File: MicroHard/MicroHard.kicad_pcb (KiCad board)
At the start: 6 copper layers, 198.2 x 104.1 mm, 193 parts, among them IC1 IS66WVO32M8DBLL-166BLI, J1 USB_B_Micro, J2 Micro_SD_Card_Det2, J3 GPIO_header, J4 MCU_Debug, J5 Controller Connector, J6 FPGA_GPIO_header, J7 FPGA_DEBUG, J8 L77HDE15SD1CH4FVGA, SW1 KMR221NGLFS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

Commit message: final fix
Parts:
- moved C35 25.1 mm to (123.2, 106.8)
- moved C44 14.4 mm to (113.4, 108.7), turned to 180 degrees
- moved C57 10.4 mm to (110.6, 95.9)
- moved C61 1.67 mm to (113.3, 101.2), turned to 90 degrees
- moved C55 0.25 mm to (114.4, 105.7)
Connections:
- U4 pad G10: +1V8 -> GND
- U4 pad G8: +1V8 -> GND
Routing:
- net +1V8: track 81.9 -> 96.7 mm
- net FPGA_CONFIG_CLOCK: track 34.2 -> 45.8 mm, vias 2 -> 4
- net FPGA_RESET: track 123.3 -> 132.5 mm
- net INIT: track 17.3 -> 25.0 mm
- net GND: track 253.8 -> 259.6 mm, vias 138 -> 136
- net Net-(U3B-PA2): track 42.9 -> 46.6 mm
- net FPGA_DONE: track 112.9 -> 115.4 mm
- net +3.3V: track 170.4 -> 172.8 mm
- net /FPGA/Unit A/Flash Memory/FLASH_CS#: track 20.1 -> 21.4 mm
- net +1V0: track 52.9 -> 53.3 mm, vias 18 -> 19

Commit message: Final changes
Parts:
- J4: footprint Connector_PinHeader_1.00mm:PinHeader_2x10_P1.00mm_Vertical -> Connector_IDC:IDC-Header_2x10_P2.54mm_Vertical
- moved R15 11.8 mm to (217.7, 77.9)
- moved SW3 11.8 mm to (212.7, 77.9)
- moved J3 10.3 mm to (229.5, 126.9)
- moved J4 9.13 mm to (225.2, 77.3)
- moved C82 5.95 mm to (219.0, 136.8)
- moved J2 5.95 mm to (223.8, 138.8)
- moved R78 5.95 mm to (212.3, 133.6)
- moved R77 5.45 mm to (211.2, 145.5), turned to 180 degrees
- moved J5 4.25 mm to (187.9, 144.8)
- moved C10 3.05 mm to (52.9, 143.3)
- moved C11 3.05 mm to (49.6, 143.3)
- moved C13 3.05 mm to (53.8, 138.8)
- moved C14 3.05 mm to (53.9, 131.8)
- moved C15 3.05 mm to (70.1, 143.3)
- moved C16 3.05 mm to (66.3, 143.3)
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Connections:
- U4 pad G10: GND -> +1V8
- U4 pad G8: GND -> +1V8
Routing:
- net Net-(J3-Pin_7): track 25.3 -> 33.2 mm
- net SD_US2_CLK: track 42.5 -> 48.7 mm
- net SD_US2_RX: track 44.7 -> 50.8 mm
- net SD_US2_CS: track 42.7 -> 48.7 mm
- net SD_US2_TX: track 42.7 -> 48.7 mm
- net Net-(U3B-PB14): track 12.0 -> 16.7 mm
- net US1_CS: track 43.0 -> 47.6 mm
- net US1_CLK: track 43.4 -> 48.1 mm
- net Net-(J6-Pin_2): track 49.0 -> 44.3 mm
- net Net-(J3-Pin_6): track 28.7 -> 33.3 mm
- net Net-(J3-Pin_5): track 29.2 -> 33.5 mm
- net Controller_Btn1: track 26.8 -> 31.1 mm
- net Controller_Z: track 33.1 -> 37.4 mm
- net Controller_X: track 34.1 -> 38.4 mm
- net Controller_Y: track 32.8 -> 37.0 mm
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- added copper zone on F.Cu, net GND
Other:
- board size 198.2 x 104.1 mm -> 197.5 x 107.7 mm
- board text added: "*"

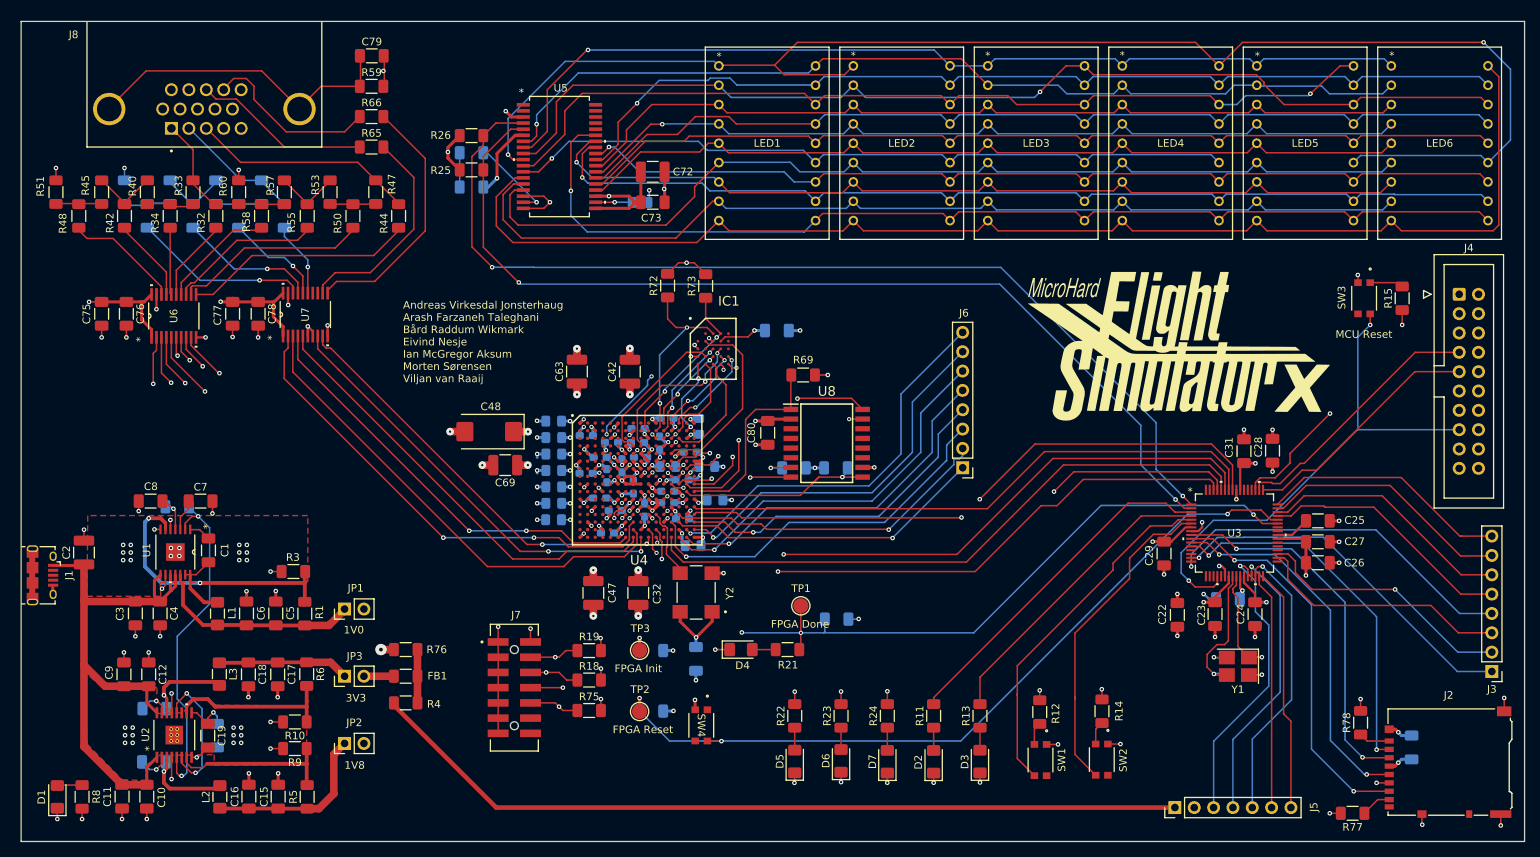
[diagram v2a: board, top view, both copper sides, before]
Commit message: Change inductor footprint
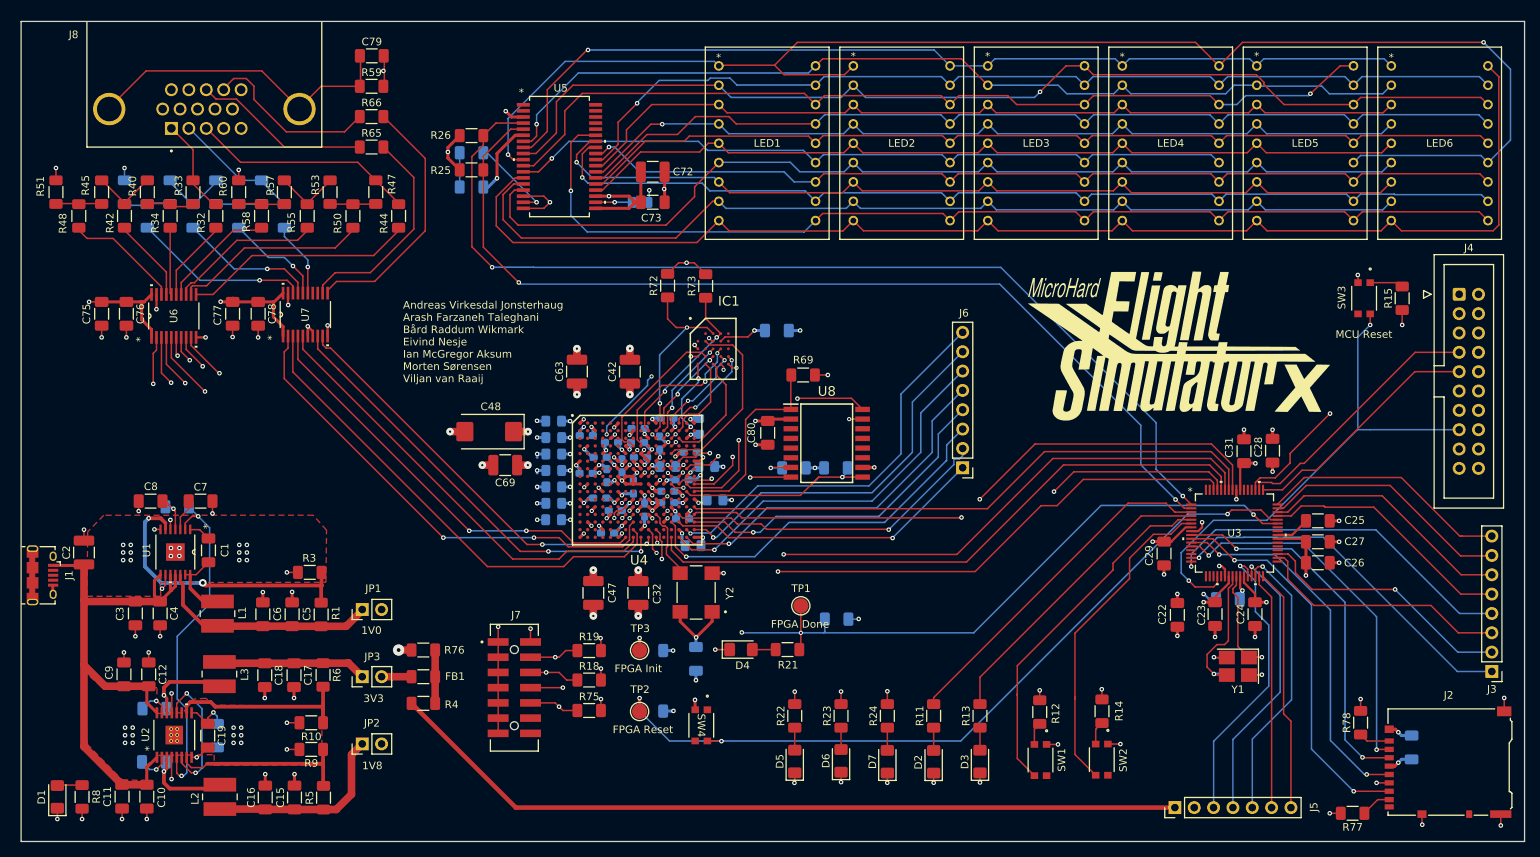
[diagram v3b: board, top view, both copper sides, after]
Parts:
- L1, L2, L3: footprint Inductor_SMD:L_1206_3216Metric_Pad1.42x1.75mm_HandSolder -> 74438357022 Wuerth Inductor:IND_8357022_WRE
- moved JP1 2.32 mm to (81.2, 118.7)
- moved JP2 2.32 mm to (81.2, 136.4)
- moved JP3 2.32 mm to (81.2, 127.6)
- moved FB1 2.32 mm to (89.2, 127.6)
- moved R4 2.32 mm to (89.2, 131.1)
- moved R76 2.32 mm to (89.2, 124.1)
- moved C15 2.15 mm to (72.3, 143.4)
- moved C16 2.15 mm to (68.4, 143.4)
- moved R10 2.15 mm to (74.5, 133.6)
- moved R9 2.15 mm to (74.5, 137.1)
- moved C17 2.15 mm to (72.2, 127.4)
- moved C18 2.15 mm to (68.3, 127.4)
- moved C5 2.15 mm to (71.9, 119.4)
- moved C6 2.15 mm to (68.1, 119.4)
- moved R1 2.15 mm to (75.8, 119.4)
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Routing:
- net Net-(JP2-A): track 23.0 -> 26.4 mm
- net Net-(JP1-A): track 27.4 -> 30.3 mm
- net Net-(JP3-A): track 17.2 -> 19.8 mm
- net +3.3VA: track 108.1 -> 105.6 mm
- net Net-(U1-PG): track 35.7 -> 38.1 mm
- net Net-(U2-VFB1): track 21.8 -> 24.0 mm
- net Net-(U2-VFB2): track 22.2 -> 24.0 mm
- net +1V0: track 55.7 -> 54.8 mm
- net +1V8: track 99.7 -> 100.5 mm
- net Net-(U2-SW2): track 13.5 -> 12.8 mm

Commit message: Small fixes
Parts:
- C79: footprint Capacitor_SMD:C_1206_3216Metric_Pad1.33x1.80mm_HandSolder -> Capacitor_SMD:C_0805_2012Metric_Pad1.18x1.45mm_HandSolder
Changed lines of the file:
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@@
 		)
 		(fp_text user "*"
-			(at -0.0112 -1.3 0)
+			(at -0.0212 -1.47 0)
 			(layer "F.SilkS")
 			(effects
@@
 		(fp_text user "*"
 			(at 0 -1.693333 0)
-			(unlocked yes)
 			(layer "F.Fab")
 			(effects
@@
 		(fp_text user "*"
 			(at 0 -1.693333 0)
+			(unlocked yes)
 			(layer "F.Fab")
 			(effects
@@
 		)
 		(fp_text user "*"
-			(at -0.0316 -1.1 0)
+			(at 0.0284 -1.21 0)
 			(layer "F.SilkS")
 			(effects
@@
 			)
 		)
-		(fp_text user "${REFERENCE}"
-			(at 6.35 10.16 0)
+		(fp_text user "*"
+			(at 0 -1.693333 0)
 			(unlocked yes)
 			(layer "F.Fab")
@@
 		(fp_text user "*"
 			(at 0 -1.693333 0)
-			(unlocked yes)
 			(layer "F.Fab")
 			(effects
@@
 			)
 		)
-		(fp_text user "*"
-			(at 0 -1.693333 0)
+		(fp_text user "${REFERENCE}"
+			(at 6.35 10.16 0)
+			(unlocked yes)
 			(layer "F.Fab")
 			(effects
@@
 		)
 		(fp_text user "*"
-			(at -0.0188 -1.2 0)
+			(at -0.0188 -1.47 0)
 			(layer "F.SilkS")
 			(effects
@@
 		(fp_text user "*"
 			(at 0 -1.693333 0)
+			(unlocked yes)
 			(layer "F.Fab")
 			(effects
@@
 		(fp_text user "*"
 			(at 0 -1.693333 0)
-			(unlocked yes)
 			(layer "F.Fab")
 			(effects
@@
 		)
 		(fp_text user "*"
-			(at -0.0036 -1.11 0)
+			(at -0.0436 -1.3 0)
 			(layer "F.SilkS")
 			(effects
@@
 			)
 		)
-		(fp_text user "*"
-			(at 0 -1.693333 0)
+		(fp_text user "${REFERENCE}"
+			(at 6.35 10.16 0)
 			(unlocked yes)
 			(layer "F.Fab")
@@
 		(fp_text user "*"
 			(at 0 -1.693333 0)
+			(unlocked yes)
 			(layer "F.Fab")
 			(effects
@@
 			)
 		)
-		(fp_text user "${REFERENCE}"
-			(at 6.35 10.16 0)
-			(unlocked yes)
+		(fp_text user "*"
+			(at 0 -1.693333 0)
 			(layer "F.Fab")
 			(effects
@@
 		)
 		(fp_text user "*"
-			(at -0.014 -1.27 0)
-			(unlocked yes)
+			(at 0 -1.31 0)
 			(layer "F.SilkS")
 			(effects
@@
 		)
 		(fp_text user "*"
-			(at -0.0164 -1.27 0)
+			(at -0.0164 -1.42 0)
 			(layer "F.SilkS")
 			(effects
@@
 		(fp_text user "*"
 			(at 0 -1.693333 0)
+			(unlocked yes)
 			(layer "F.Fab")
 			(effects
@@
 			)
 		)
-		(fp_text user "${REFERENCE}"
-			(at 6.35 10.16 0)
-			(unlocked yes)
+		(fp_text user "*"
+			(at 0 -1.693333 0)
 			(layer "F.Fab")
 			(effects
@@
 			)
 		)
-		(fp_text user "*"
-			(at 0 -1.693333 0)
+		(fp_text user "${REFERENCE}"
+			(at 6.35 10.16 0)
 			(unlocked yes)
 			(layer "F.Fab")
@@
 		)
 	)
-	(footprint "Capacitor_SMD:C_1206_3216Metric_Pad1.33x1.80mm_HandSolder"
+	(footprint "Capacitor_SMD:C_0805_2012Metric_Pad1.18x1.45mm_HandSolder"
 		(layer "F.Cu")
 		(at 82.405 46.0225)
-		(descr "Capacitor SMD 1206 (3216 Metric), square (rectangular) end terminal, IPC_7351 nominal with elongated pad for handsoldering. (Body size source: IPC-SM-782 page 76, https://www.pcb-3d.com/wordpress/wp-content/uploads/ipc-sm-782a_amendment_1_and_2.pdf), generated with kicad-footprint-generator")
+		(descr "Capacitor SMD 0805 (2012 Metric), square (rectangular) end terminal, IPC_7351 nominal with elongated pad for handsoldering. (Body size source: IPC-SM-782 page 76, https://www.pcb-3d.com/wordpress/wp-content/uploads/ipc-sm-782a_amendment_1_and_2.pdf, https://docs.google.com/spreadsheets/d/1BsfQQcO9C6DZCsRaXUlFlo91Tg2WpOkGARC1WS5S8t0/edit?usp=sharing), generated with kicad-footprint-generator")
 		(tags "capacitor handsolder")
 		(property "Reference" "C79"
-			(at 0 -1.85 0)
+			(at 0 -1.68 0)
 			(layer "F.SilkS")
 			(effects
@@
 		)
 		(property "Value" "4p"
-			(at 0 1.85 0)
+			(at 0 1.68 0)
 			(layer "F.Fab")
 			(effects
@@
 			)
 		)
-		(property "Footprint" "Capacitor_SMD:C_1206_3216Metric_Pad1.33x1.80mm_HandSolder"
+		(property "Footprint" "Capacitor_SMD:C_0805_2012Metric_Pad1.18x1.45mm_HandSolder"
 			(at 0 0 0)
 			(unlocked yes)
@@
 		(attr smd)
 		(fp_line
-			(start -0.711252 -0.91)
-			(end 0.711252 -0.91)
+			(start -0.261252 -0.735)
+			(end 0.261252 -0.735)
 			(stroke
 				(width 0.12)
@@
 		)
 		(fp_line
-			(start -0.711252 0.91)
-			(end 0.711252 0.91)
+			(start -0.261252 0.735)
+			(end 0.261252 0.735)
 			(stroke
 				(width 0.12)
@@
 		)
 		(fp_line
-			(start -2.48 -1.15)
-			(end 2.48 -1.15)
+			(start -1.88 -0.98)
+			(end 1.88 -0.98)
 			(stroke
 				(width 0.05)
@@
 		)
 		(fp_line
-			(start -2.48 1.15)
-			(end -2.48 -1.15)
+			(start -1.88 0.98)
+			(end -1.88 -0.98)
 			(stroke
 				(width 0.05)
@@
 		)
 		(fp_line
-			(start 2.48 -1.15)
-			(end 2.48 1.15)
+			(start 1.88 -0.98)
+			(end 1.88 0.98)
 			(stroke
 				(width 0.05)
@@
 		)
 		(fp_line
-			(start 2.48 1.15)
-			(end -2.48 1.15)
+			(start 1.88 0.98)
+			(end -1.88 0.98)
 			(stroke
 				(width 0.05)
@@
 		)
 		(fp_line
-			(start -1.6 -0.8)
-			(end 1.6 -0.8)
+			(start -1 -0.625)
+			(end 1 -0.625)
 			(stroke
 				(width 0.1)
@@
 		)
 		(fp_line
-			(start -1.6 0.8)
-			(end -1.6 -0.8)
+			(start -1 0.625)
+			(end -1 -0.625)
 			(stroke
 				(width 0.1)
@@
 		)
 		(fp_line
-			(start 1.6 -0.8)
-			(end 1.6 0.8)
+			(start 1 -0.625)
+			(end 1 0.625)
 			(stroke
 				(width 0.1)
@@
 		)
 		(fp_line
-			(start 1.6 0.8)
-			(end -1.6 0.8)
+			(start 1 0.625)
+			(end -1 0.625)
 			(stroke
 				(width 0.1)
@@
 			(effects
 				(font
-					(size 0.8 0.8)
-					(thickness 0.12)
+					(size 0.5 0.5)
+					(thickness 0.08)
 				)
 			)
 		)
 		(pad "1" smd roundrect
-			(at -1.5625 0)
-			(size 1.325 1.8)
+			(at -1.0375 0)
+			(size 1.175 1.45)
 			(layers "F.Cu" "F.Paste" "F.Mask")
-			(roundrect_rratio 0.188679)
+			(roundrect_rratio 0.212766)
 			(net 19 "Net-(J8-SHIELD)")
 			(pintype "passive")
 		)
 		(pad "2" smd roundrect
-			(at 1.5625 0)
-			(size 1.325 1.8)
+			(at 1.0375 0)
+			(size 1.175 1.45)
 			(layers "F.Cu" "F.Paste" "F.Mask")
-			(roundrect_rratio 0.188679)
+			(roundrect_rratio 0.212766)
 			(net 2 "GND")
 			(pintype "passive")
 		)
-		(model "${KICAD8_3DMODEL_DIR}/Capacitor_SMD.3dshapes/C_1206_3216Metric.wrl"
+		(model "${KICAD8_3DMODEL_DIR}/Capacitor_SMD.3dshapes/C_0805_2012Metric.wrl"
 			(offset
 				(xyz 0 0 0)
@@
 	)
 	(segment
+		(start 83.4425 46.0225)
+		(end 83.925 46.505)
+		(width 0.2)
+		(layer "F.Cu")
+		(net 2)
+	)
+	(segment
 		(start 125.875 109.25)
 		(end 124.75 109.25)
@@
 	)
 	(segment
+		(start 83.925 46.505)
+		(end 83.925 48)
+		(width 0.2)
+		(layer "F.Cu")
+		(net 2)
+	)
+	(segment
 		(start 67.475 83)
 		(end 67.475 81.4625)
@@
 	)
 	(segment
-		(start 84.04945 46.0225)
-		(end 84.04945 47.87555)
-		(width 0.2)
-		(layer "F.Cu")
-		(net 2)
-	)
-	(segment
 		(start 193.150002 122.3441)
 		(end 193.150001 122.344101)
@@
 	)
 	(segment
-		(start 84.04945 47.87555)
-		(end 83.925 48)
-		(width 0.2)
-		(layer "F.Cu")
-		(net 2)
-	)
-	(segment
 		(start 114.76 103.25)
 		(end 114.75 103.25)
@@
 	)
 	(segment
-		(start 75.73425 50.0225)
-		(end 72.85425 52.9025)
+		(start 80.92445 46.46555)
+		(end 80.92445 49.9725)
 		(width 0.2)
 		(layer "F.Cu")
@@
 	)
 	(segment
-		(start 80.92445 46.0225)
-		(end 80.92445 49.9725)
+		(start 67.95175 48)
+		(end 52.76675 48)
 		(width 0.2)
 		(layer "F.Cu")
@@
 	)
 	(segment
-		(start 80.87445 50.0225)
-		(end 75.73425 50.0225)
+		(start 81.3675 46.0225)
+		(end 80.92445 46.46555)
 		(width 0.2)
 		(layer "F.Cu")
@@
 	)
 	(segment
-		(start 52.76675 48)
-		(end 47.86425 52.9025)
+		(start 75.73425 50.0225)
+		(end 72.85425 52.9025)
 		(width 0.2)
 		(layer "F.Cu")
@@
 	)
 	(segment
-		(start 72.85425 52.9025)
-		(end 67.95175 48)
+		(start 80.87445 50.0225)
+		(end 75.73425 50.0225)
 		(width 0.2)
 		(layer "F.Cu")
@@
 	)
 	(segment
-		(start 67.95175 48)
-		(end 52.76675 48)
+		(start 52.76675 48)
+		(end 47.86425 52.9025)
+		(width 0.2)
+		(layer "F.Cu")
+		(net 19)
+	)
+	(segment
+		(start 72.85425 52.9025)
+		(end 67.95175 48)
 		(width 0.2)
 		(layer "F.Cu")
